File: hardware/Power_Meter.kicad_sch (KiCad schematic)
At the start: 36 parts, among them J5 Screw_Terminal_01x02, J6 Conn_01x10, J7 Conn_01x10, Q1 SISS73DN, U3 ADG659, U7 TPS65133DPDR, U8 TPS7A3901DSCR, U9 PLMR51420XDDCR

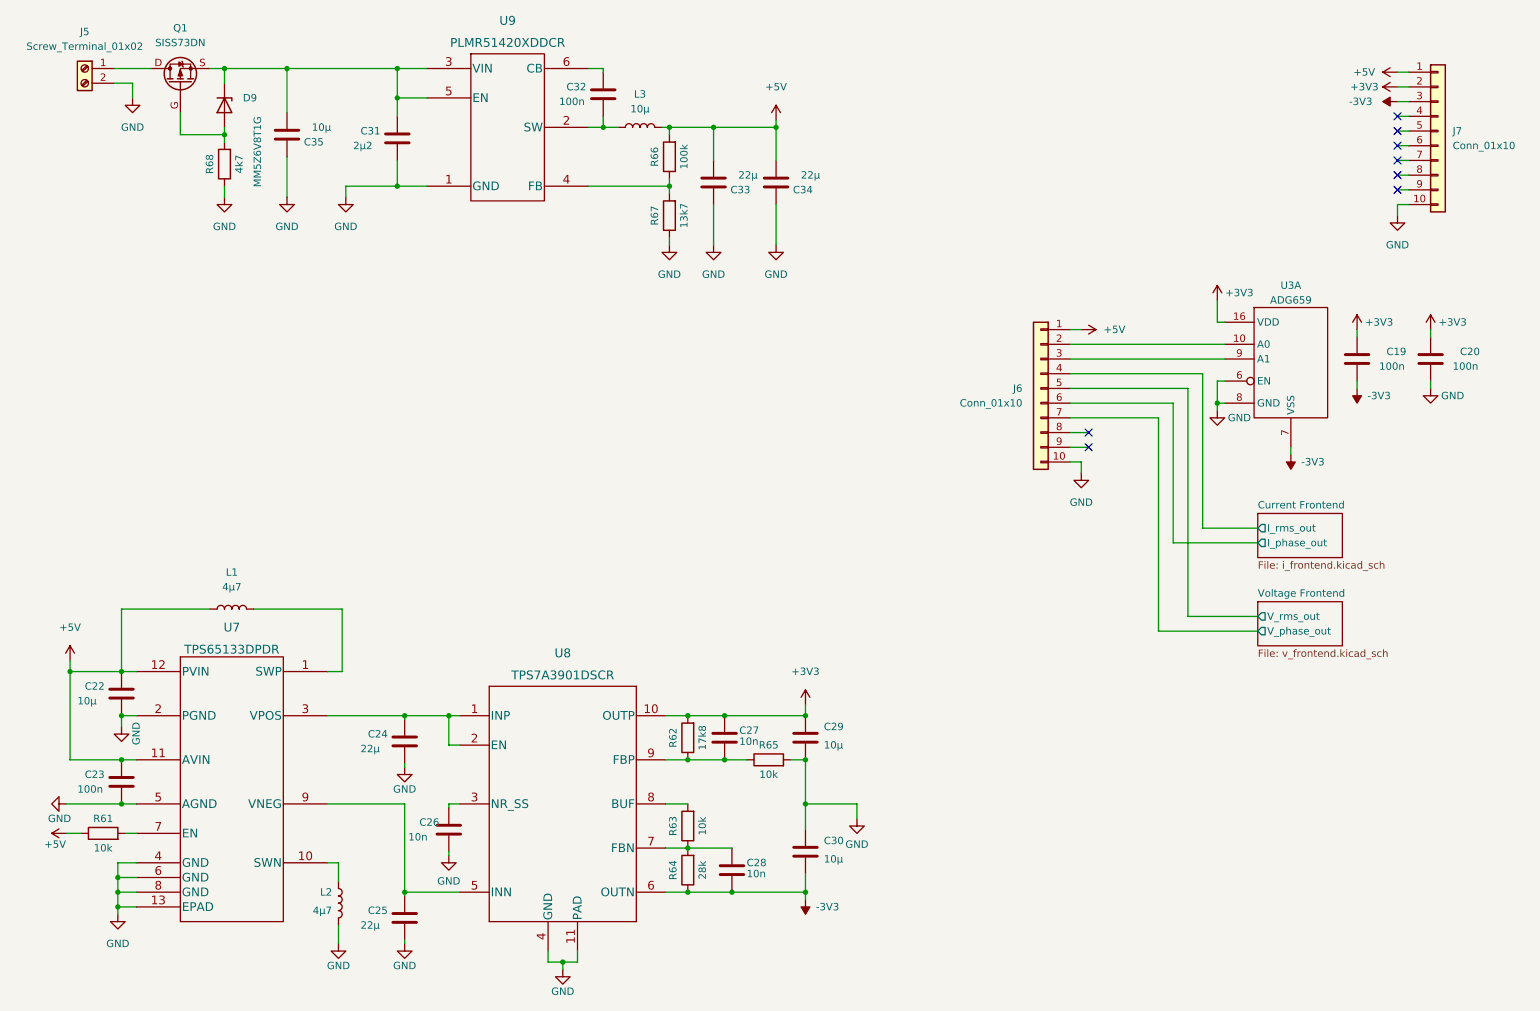
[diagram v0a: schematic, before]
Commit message: Adding .pdf exports
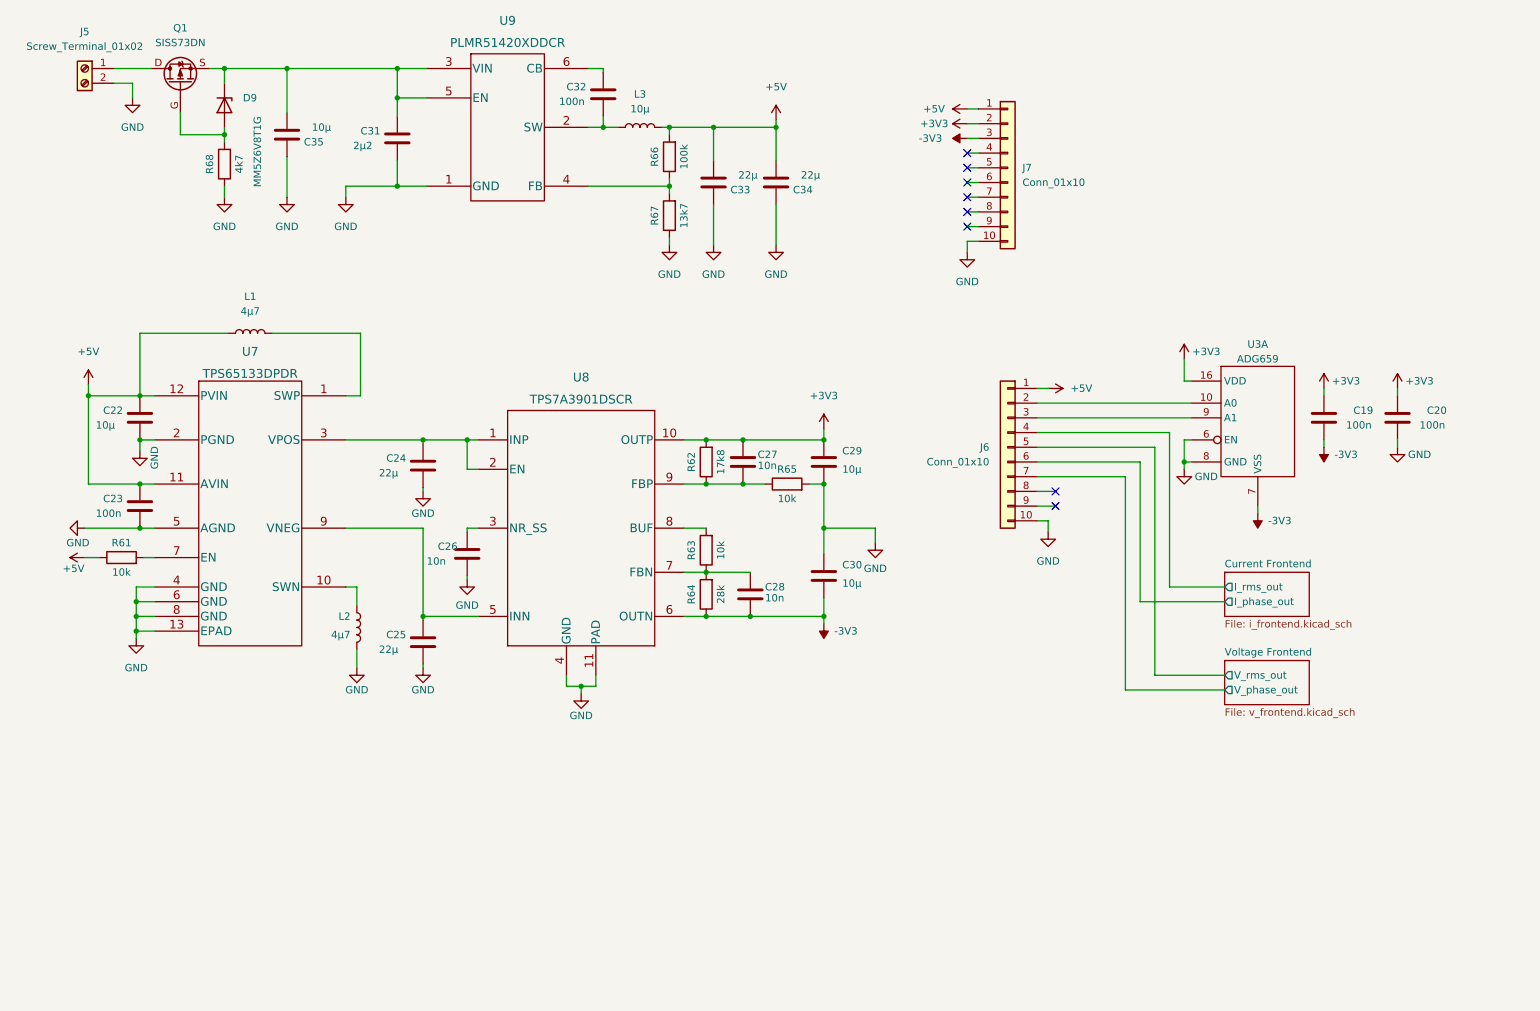
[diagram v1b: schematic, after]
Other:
- moved on the sheet: C19, C20, C22, C23, C24, C25, C26, C27, C28, C29, C30, J6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
